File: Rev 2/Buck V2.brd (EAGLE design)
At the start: 77.5 x 51.1 mm, 51 parts, among them Q1 IRF3205STRLPBF, Q2 IRF3205STRLPBF, Q3 IRF3205STRLPBF, Q4 IRF3205STRLPBF, U1 Value

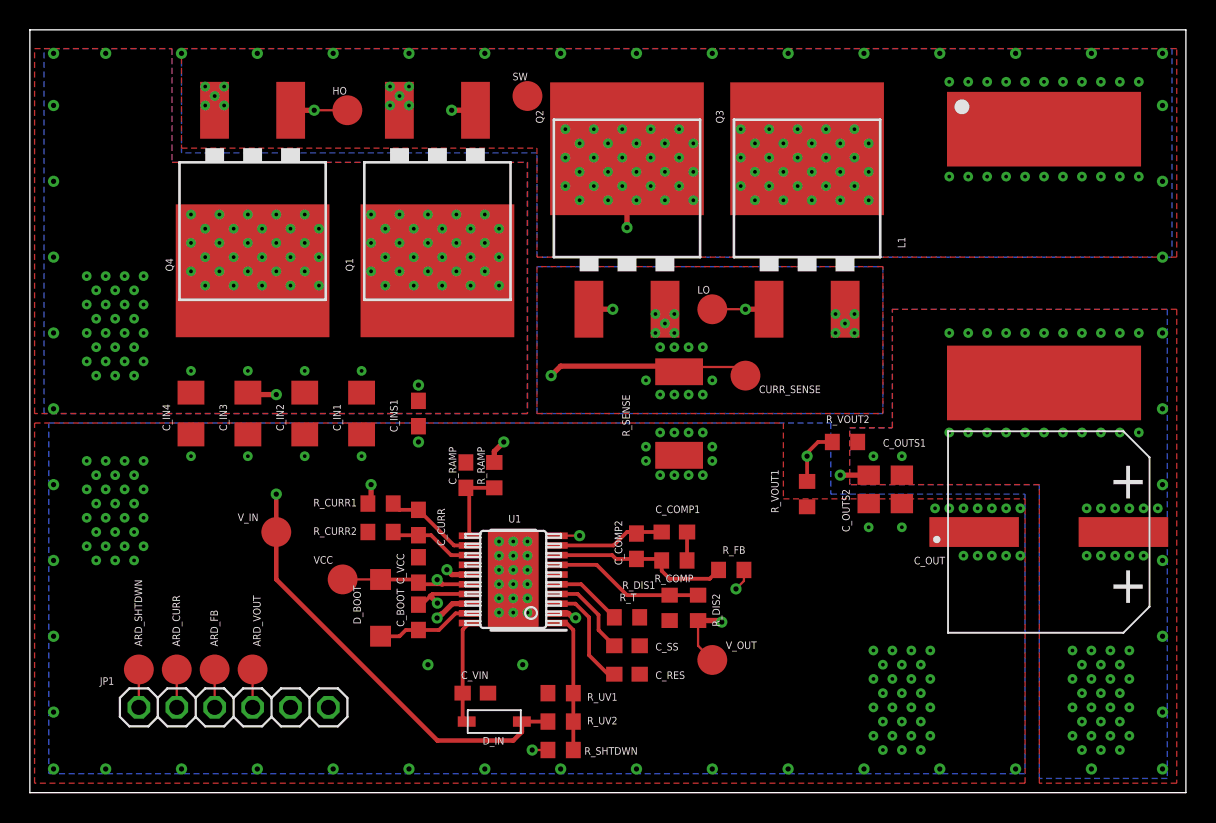
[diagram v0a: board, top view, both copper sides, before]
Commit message: Finished evreything, boards ordered from JLC! Hi Thomas
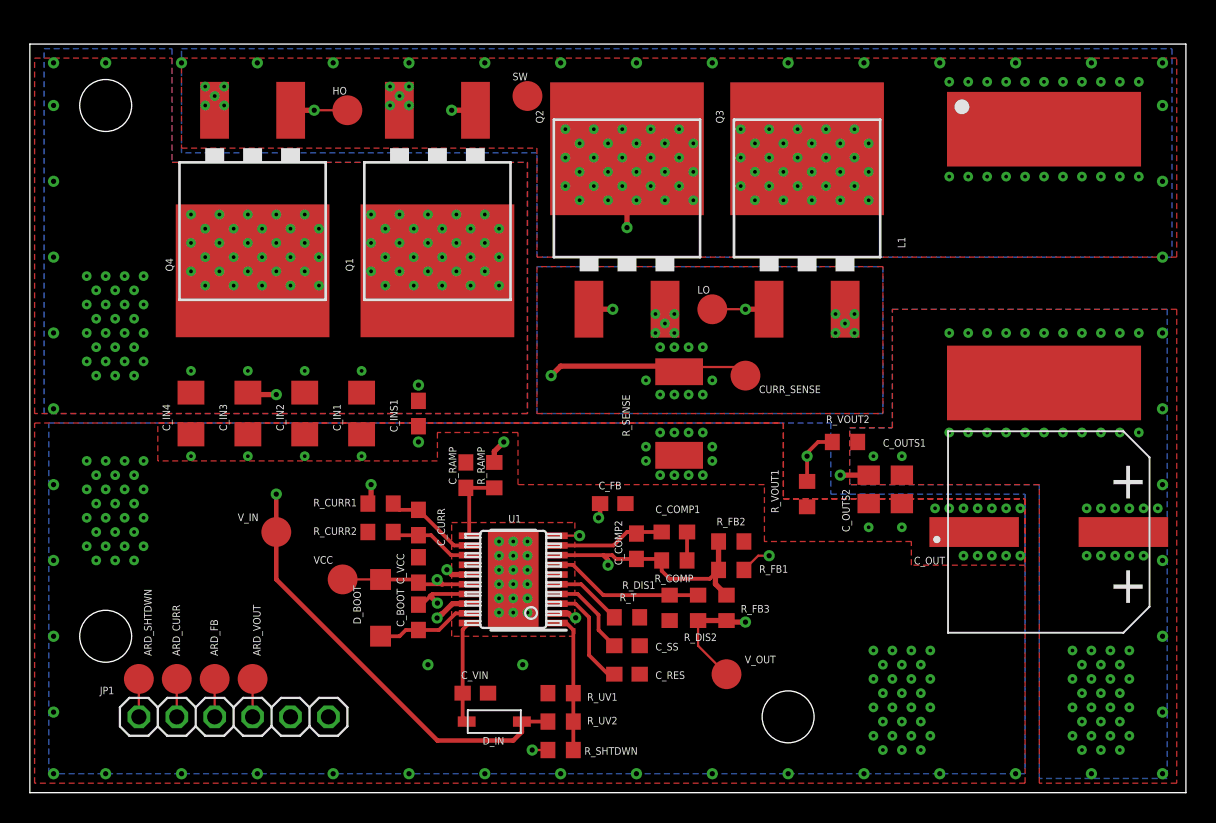
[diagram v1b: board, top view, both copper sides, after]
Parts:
- added C_FB: 0.68 uF, rcl:C0603
- added R_FB2: 10 K, rcl:R0603
- added R_FB3: 178 K, rcl:R0603
- R_FB1: value 1 K -> 17 K
- moved V_OUT 1.35 mm to (46.7, 7.62)
- moved ARD_CURR 0.63 mm to (9.84, 7.30)
- moved ARD_FB 0.63 mm to (12.4, 7.30)
- moved ARD_SHTDWN 0.63 mm to (7.30, 7.30)
- moved ARD_VOUT 0.63 mm to (14.9, 7.30)
- moved JP1 0.63 mm to (13.7, 4.76)
- renumbered R_FB to R_FB1
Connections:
- net GND: now also C_FB.2, R_FB2.1
- net N$15: now also C_FB.1, R_FB2.2, R_FB3.1
- net V_OUT: now also R_FB3.2
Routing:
- net N$15: track 12.1 -> 21.0 mm, vias 0 -> 2
- net ARD_FEEDBACK: track 44.7 -> 49.1 mm
- net V_OUT: track 20.4 -> 22.0 mm
- net ARD_VOUT: track 56.0 -> 56.7 mm
- net ARD_SHUTDOWN: track 32.1 -> 31.4 mm
- net ARD_CURRENT: track 42.4 -> 43.0 mm
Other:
- board size 77.5 x 51.1 mm -> 77.5 x 50.2 mm
